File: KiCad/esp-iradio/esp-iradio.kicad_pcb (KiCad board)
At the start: 4 copper layers, 90 x 60 mm, 120 parts, among them J201 USB-C TYPE-C-31-M-12, J202 Li-Po cell (JST-PH), J3 Display HS20S010B CN1, J4 microSD push-push TF-01A, J5 Line out 3.5mm PJ-320D, J6 Speaker 4-8 Ohm, J7 Display CN2 (mechanical), Q201 MMBT3904, Q202 MMBT3904, Q203 DMG2305UX-7, SW1 EC11 with switch, SW201 RESET, SW202 BOOT, SW203 ON/OFF MSK12C02, U1 PCM5102APWR, U2 MAX98357AETE+T, U201 BQ24074RGTR, U202 USBLC6-2SC6, U203 CH340C, U204 DW01A, U205 FS8205A, U206 AP7361C-33Y5-13, U207 TPLP5907MFX-3.3, U3 ESP32-WROVER-IE-N16R8

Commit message: BQ24074RGTT (C2861252) for U201, one BOM line per LCSC part
Co-Authored-By: Claude Opus 5.5 <noreply@anthropic.com>
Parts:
- U201: value BQ24074RGTR -> BQ24074RGTT
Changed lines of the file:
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@@
 			)
 		)
-		(property "Value" "BQ24074RGTR"
+		(property "Value" "BQ24074RGTT"
 			(at 0 2.83 0)
 			(layer "F.Fab")
@@
 			)
 		)
-		(property "LCSC" "C54313"
+		(property "LCSC" "C2861252"
 			(at 0 0 0)
 			(layer "F.SilkS")

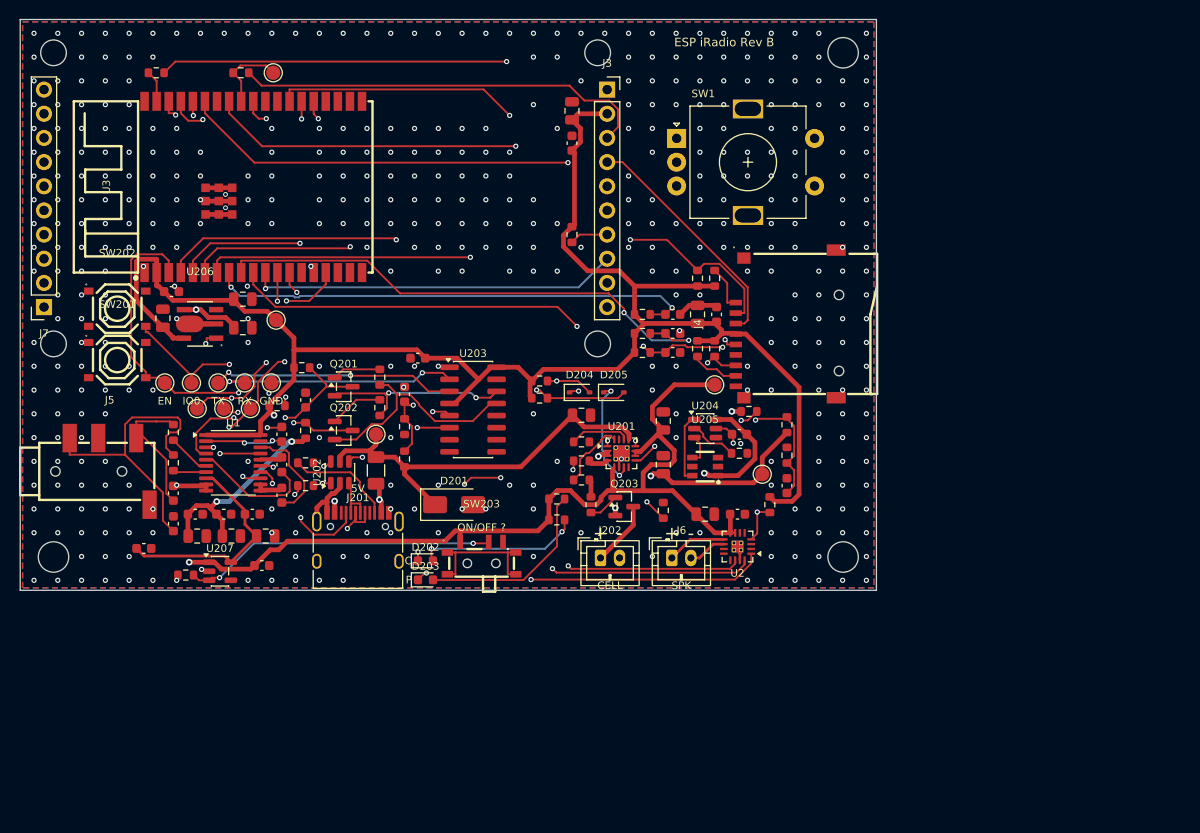
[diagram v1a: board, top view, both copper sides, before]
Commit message: KiCad Rev C: hand assembly (1206), RCA outputs, display/encoder/connectors floor plan
Co-Authored-By: Claude Opus 5.5 <noreply@anthropic.com>
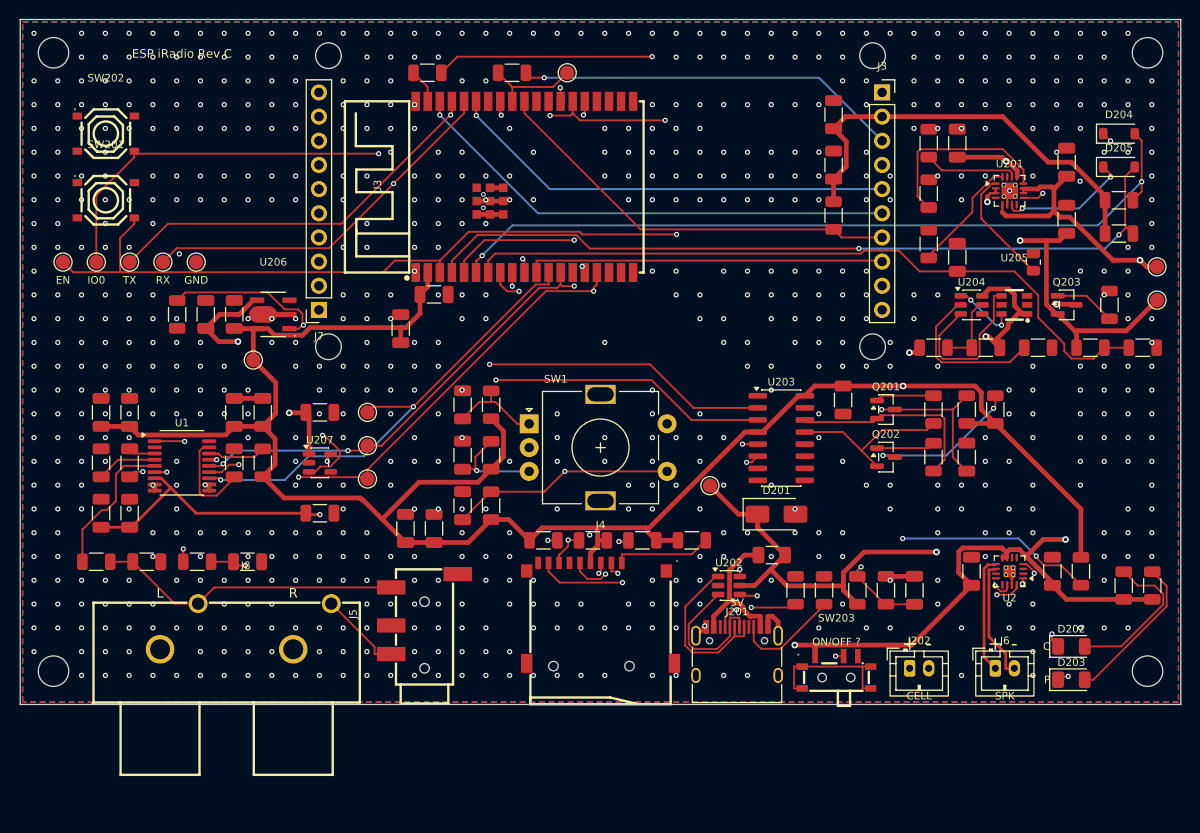
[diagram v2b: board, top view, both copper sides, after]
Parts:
- added H8: M3, MountingHole:MountingHole_3.2mm_M3, F.Cu at (103.5, 103.5)
- added J8: Line out RCA L/R AV-210-WR, lcsc:RCA-TH_AV-210-WR, F.Cu at (123.7, 163.8)
- C10, C12, C14, C201, C202, C203, C208, C209, C210, C22, C3, C5: footprint Capacitor_SMD:C_0805_2012Metric -> Capacitor_SMD:C_1206_3216Metric
- C11, C13, C15, C16, C17, C18, C19, C204, C205, C206, C207, C211, C212, C213, C214, C23, C25, C4, C6, C7, C8, C9: footprint Capacitor_SMD:C_0603_1608Metric -> Capacitor_SMD:C_1206_3216Metric
- D202, D203: footprint LED_SMD:LED_0603_1608Metric -> LED_SMD:LED_1206_3216Metric
- D204, D205: value BAT54WS -> BAT54W; footprint Diode_SMD:D_SOD-323 -> Diode_SMD:D_SOD-123
- R10, R11, R12, R15, R16, R17, R201, R202, R203, R204, R205, R206, R207, R208, R209, R21, R210, R211, R212, R213, R214, R215, R216, R217, R218, R219, R220, R221, R3, R4, R5, R6, R7, R8, R9: footprint Resistor_SMD:R_0603_1608Metric -> Resistor_SMD:R_1206_3216Metric
- RT201: footprint Resistor_SMD:R_0603_1608Metric -> Resistor_SMD:R_0805_2012Metric
- moved R208 72.5 mm to (202.5, 141.0)
- moved R207 70.0 mm to (199.5, 141.0), turned to 90 degrees
- moved C205 69.8 mm to (199.5, 146.0)
- moved D203 68.7 mm to (210.5, 169.4)
- moved D202 68.5 mm to (210.5, 165.9)
- moved R213 63.8 mm to (215.5, 119.0)
- moved R215 63.3 mm to (215.5, 122.5)
- moved R214 63.3 mm to (219.0, 159.5), turned to 90 degrees
- moved D204 62.9 mm to (215.5, 112.0)
- moved R212 60.0 mm to (216.0, 159.5), turned to 90 degrees
- moved R206 58.4 mm to (196.0, 146.0)
- moved R216 58.4 mm to (214.5, 130.0)
- moved R205 58.3 mm to (196.0, 141.0)
- moved D205 58.1 mm to (215.5, 115.5)
- moved C214 57.4 mm to (194.0, 160.0)
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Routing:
- net VSYS: track 128.2 -> 206.4 mm, vias 2 -> 5
- net +3V3: track 202.7 -> 278.2 mm, vias 3 -> 1
- net ESP_EN: track 46.3 -> 120.2 mm
- net ESP_IO0: track 60.3 -> 134.1 mm, vias 3 -> 5
- net /Power, charger and USB/VIN: track 42.9 -> 97.5 mm, vias 0 -> 2
- net Net-(U1-BCK): track 88.9 -> 133.0 mm, vias 5 -> 3
- net TXD0: track 57.3 -> 100.7 mm, vias 3 -> 2
- net Net-(C6-+): track 70.3 -> 27.7 mm, vias 2 -> 1
- net /Power, charger and USB/EN_3V3: track 59.7 -> 101.1 mm
- net Net-(U1-LRCK): track 84.8 -> 125.8 mm
- net Net-(C7-+): track 73.1 -> 32.3 mm
- net Net-(J3-Pin_4): track 76.5 -> 116.9 mm, vias 1 -> 2
- net RXD0: track 56.5 -> 92.6 mm, vias 3 -> 2
- net Net-(U1-DIN): track 91.2 -> 126.4 mm, vias 5 -> 4
- net CHG: track 50.8 -> 82.3 mm
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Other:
- board size 90 x 60 mm -> 122 x 72 mm
- board text added: "ESP iRadio Rev C"
- board text added: "L"
- board text added: "R"
- board text removed: "ESP iRadio Rev B"

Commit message: Rev C review round 7: switch off the USB-C, 1206 pitch, RCA pinout confirmed
Co-Authored-By: Claude Opus 5.5 <noreply@anthropic.com>
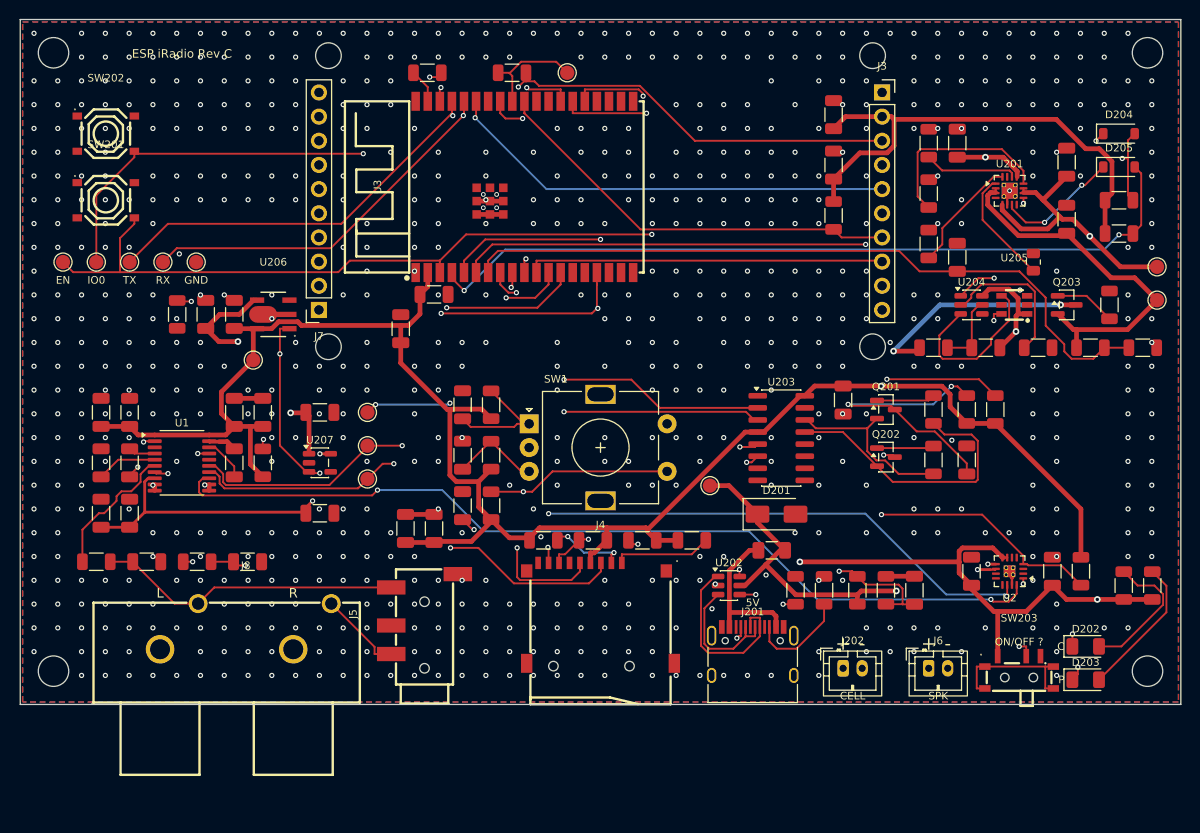
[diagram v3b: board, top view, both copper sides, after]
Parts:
- moved SW203 19.2 mm to (205.0, 168.6)
- moved J202 7.00 mm to (186.5, 168.2)
- moved J6 7.00 mm to (195.5, 168.2)
- moved J201 1.65 mm to (177.0, 167.9)
- moved D202 1.50 mm to (212.0, 165.9)
- moved D203 1.50 mm to (212.0, 169.4)
- moved F201 0.50 mm to (179.0, 155.8)
- moved C205 0.30 mm to (199.5, 146.3)
- moved R206 0.30 mm to (196.0, 146.3)
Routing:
- net /Power, charger and USB/EN_3V3: track 101.1 -> 117.8 mm, vias 3 -> 4
- net Net-(Q202-E): track 17.8 -> 30.0 mm
- net Net-(J3-Pin_4): track 116.9 -> 128.4 mm
- net ESP_IO0: track 134.1 -> 143.5 mm, vias 5 -> 4
- net Net-(U1-DIN): track 126.4 -> 135.7 mm
- net ESP_EN: track 120.2 -> 129.4 mm, vias 2 -> 3
- net Net-(C8-+): track 49.3 -> 57.8 mm, vias 2 -> 3
- net /Power, charger and USB/VIN: track 97.5 -> 90.6 mm
- net Net-(J6-Pin_2): track 12.7 -> 18.4 mm, vias 0 -> 1
- net Net-(C17-+): track 10.2 -> 4.56 mm
- net Net-(J202-Pin_1): track 54.1 -> 59.6 mm
- net Net-(J3-Pin_3): track 101.4 -> 106.6 mm
- net Net-(C15-+): track 10.5 -> 5.48 mm
- net VBUS_SENSE: track 68.9 -> 73.9 mm
- net VSYS: track 206.4 -> 211.1 mm
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
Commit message: Rev C: parts spread for hand soldering, board 122 x 76 mm
Co-Authored-By: Claude Opus 5.5 <noreply@anthropic.com>
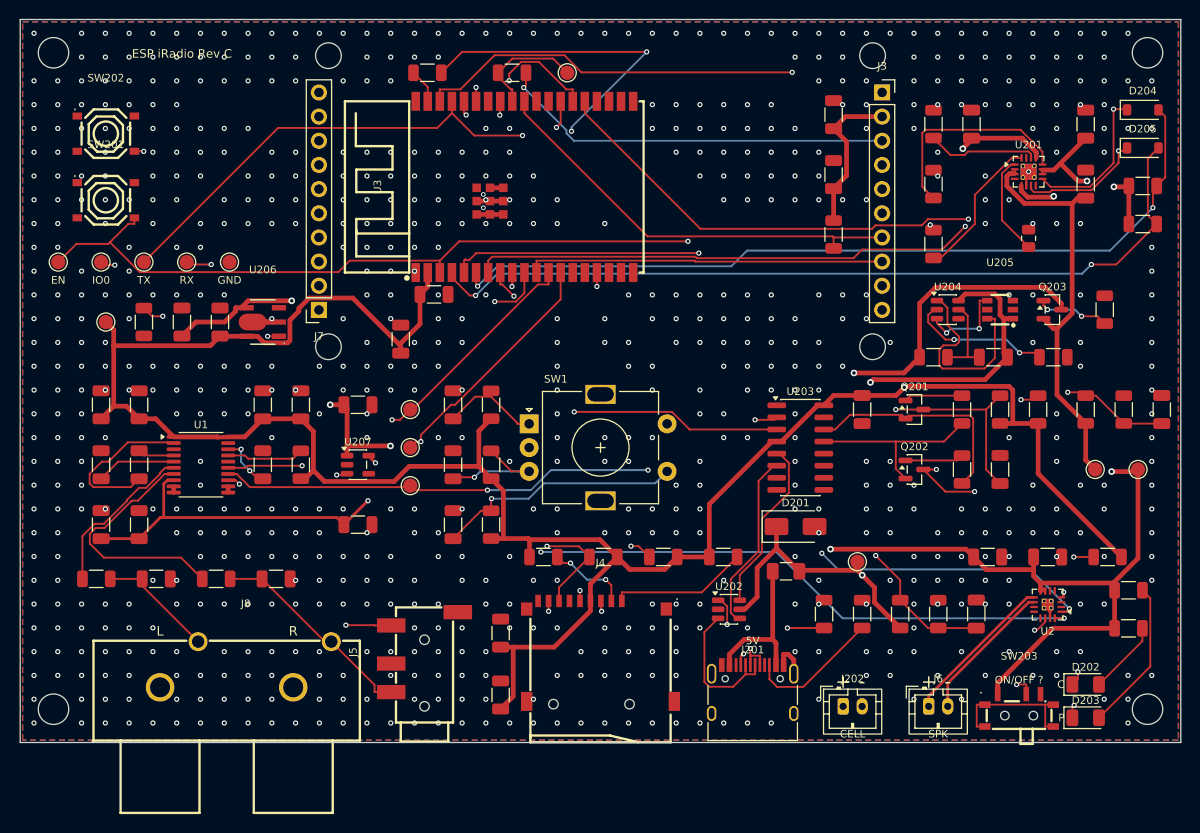
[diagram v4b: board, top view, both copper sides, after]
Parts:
- moved C207 26.8 mm to (220.0, 141.0)
- moved TP2 21.4 mm to (217.5, 147.3)
- moved TP202 18.9 mm to (213.0, 147.3)
- moved C4 18.8 mm to (150.5, 171.0)
- moved TP201 17.4 mm to (188.0, 157.0)
- moved TP4 16.0 mm to (109.0, 131.8)
- moved C3 14.9 mm to (150.5, 164.5)
- moved C214 6.96 mm to (200.5, 162.5)
- moved R218 6.80 mm to (216.0, 141.0), turned to 90 degrees
- moved R217 6.52 mm to (212.0, 141.0), turned to 90 degrees
- moved R204 6.04 mm to (196.5, 162.5)
- moved U2 5.32 mm to (208.0, 161.5)
- moved R203 5.15 mm to (192.5, 162.5)
- moved R202 4.72 mm to (188.5, 162.5)
- moved TP8 4.55 mm to (141.0, 149.0)
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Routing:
- net +3V3: track 278.2 -> 314.1 mm, vias 1 -> 2
- net /Power, charger and USB/CHG_N: track 61.0 -> 78.8 mm, vias 3 -> 2
- net Net-(U1-DIN): track 135.7 -> 121.0 mm, vias 4 -> 5
- net /Power, charger and USB/EN_3V3: track 117.8 -> 131.3 mm
- net Net-(R17-+): track 12.8 -> 25.8 mm, vias 2 -> 0
- net Net-(C15-+): track 5.48 -> 17.0 mm, vias 2 -> 0
- net Net-(U204-OD): track 10.3 -> 21.0 mm, vias 2 -> 0
- net Net-(U1-LRCK): track 123.1 -> 133.6 mm, vias 4 -> 3
- net Net-(Q202-E): track 30.0 -> 19.6 mm
- net VBUS_SENSE: track 73.9 -> 84.0 mm
- net /Power, charger and USB/PGOOD_N: track 65.4 -> 75.3 mm, vias 3 -> 2
- net ESP_IO0: track 143.5 -> 153.4 mm, vias 4 -> 6
- net VBAT_SENSE: track 76.4 -> 86.2 mm, vias 0 -> 2
- net /Power, charger and USB/USB_D+: track 19.4 -> 10.4 mm, vias 0 -> 2
- net /Power, charger and USB/BATN: track 54.1 -> 62.8 mm
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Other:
- board size 122 x 72 mm -> 122 x 76 mm

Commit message: C207 at the ADC pin (IO35), board re-routed
Co-Authored-By: Claude Opus 5.5 <noreply@anthropic.com>
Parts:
- moved C207 71.4 mm to (149.5, 129.5), turned to 0 degrees
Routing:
- net Net-(J3-Pin_4): track 119.7 -> 100.6 mm, vias 3 -> 2
- net Net-(U204-OD): track 21.0 -> 6.85 mm
- net Net-(U1-BCK): track 124.2 -> 138.3 mm
- net /Power, charger and USB/EN_3V3: track 131.3 -> 118.6 mm
- net Net-(R17-+): track 25.8 -> 13.0 mm, vias 0 -> 2
- net /Power, charger and USB/CHG_N: track 78.8 -> 66.2 mm, vias 2 -> 3
- net CHG: track 87.0 -> 97.8 mm, vias 2 -> 0
- net Net-(U1-DIN): track 121.0 -> 130.2 mm
- net Net-(J3-Pin_6): track 61.0 -> 52.1 mm
- net /Power, charger and USB/VIN: track 88.0 -> 96.8 mm, vias 2 -> 3
- net /Power, charger and USB/USB_D+: track 10.4 -> 18.9 mm, vias 2 -> 0
- net TXD0: track 101.9 -> 94.1 mm
- net /Power, charger and USB/BATN: track 62.8 -> 56.8 mm
- net Net-(Q201-E): track 24.1 -> 29.2 mm
- net VBAT_SENSE: track 86.2 -> 81.4 mm
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
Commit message: 3D models for the USB-C and the encoder (project footprints, EasyEDA models)
Co-Authored-By: Claude Opus 5.5 <noreply@anthropic.com>
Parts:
- J201: footprint Connector_USB:USB_C_Receptacle_HRO_TYPE-C-31-M-12 -> esp-iradio:USB_C_Receptacle_HRO_TYPE-C-31-M-12
- SW1: footprint Rotary_Encoder:RotaryEncoder_Alps_EC11E-Switch_Vertical_H20mm -> esp-iradio:RotaryEncoder_Alps_EC11E-Switch_Vertical_H20mm
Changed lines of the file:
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@@
 		)
 	)
-	(footprint "Connector_USB:USB_C_Receptacle_HRO_TYPE-C-31-M-12"
+	(footprint "esp-iradio:USB_C_Receptacle_HRO_TYPE-C-31-M-12"
 		(layer "F.Cu")
 		(at 177 171.9)
@@
 		)
 		(embedded_fonts no)
-		(model "${KICAD9_3DMODEL_DIR}/Connector_USB.3dshapes/USB_C_Receptacle_HRO_TYPE-C-31-M-12.step"
+		(model "${KIPRJMOD}/lib/lcsc.3dshapes/USB-C_SMD-TYPE-C-31-M-12_1.wrl"
 			(offset
-				(xyz 0 0 0)
+				(xyz 0 1.4 0)
 			)
 			(scale
@@
 			)
 			(rotate
-				(xyz 0 0 0)
+				(xyz 0 0 180)
 			)
 		)
@@
 		(embedded_fonts no)
 	)
-	(footprint "Rotary_Encoder:RotaryEncoder_Alps_EC11E-Switch_Vertical_H20mm"
+	(footprint "esp-iradio:RotaryEncoder_Alps_EC11E-Switch_Vertical_H20mm"
 		(layer "F.Cu")
 		(at 153.5 142.5)
@@
 		)
 		(embedded_fonts no)
-		(model "${KICAD9_3DMODEL_DIR}/Rotary_Encoder.3dshapes/RotaryEncoder_Alps_EC11E-Switch_Vertical_H20mm.step"
+		(model "${KIPRJMOD}/lib/lcsc.3dshapes/SW-TH_EC11XXXXXXXX-L11.7-W12.0-H24.5-P2.5-LS14.5.wrl"
 			(offset
-				(xyz 0 0 0)
+				(xyz 7.5 -2.5 0)
 			)
 			(scale
@@
 			)
 			(rotate
-				(xyz 0 0 0)
+				(xyz 0 0 -90)
 			)
 		)

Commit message: 3D: display module on J3, solid PJ-320D model
Co-Authored-By: Claude Opus 5.5 <noreply@anthropic.com>
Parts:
- J3: footprint Connector_PinSocket_2.54mm:PinSocket_1x10_P2.54mm_Vertical -> esp-iradio:PinSocket_1x10_P2.54mm_Vertical_HS20S010B
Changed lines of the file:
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@@
 		)
 	)
-	(footprint "Connector_PinSocket_2.54mm:PinSocket_1x10_P2.54mm_Vertical"
+	(footprint "esp-iradio:PinSocket_1x10_P2.54mm_Vertical_HS20S010B"
 		(layer "F.Cu")
 		(at 190.6 107.67)
@@
 			(offset
 				(xyz 0 0 0)
+			)
+			(scale
+				(xyz 1 1 1)
+			)
+			(rotate
+				(xyz 0 0 0)
+			)
+		)
+		(model "${KIPRJMOD}/lib/esp-iradio.3dshapes/HS20S010B_on_sockets.wrl"
+			(offset
+				(xyz 0 0 0)

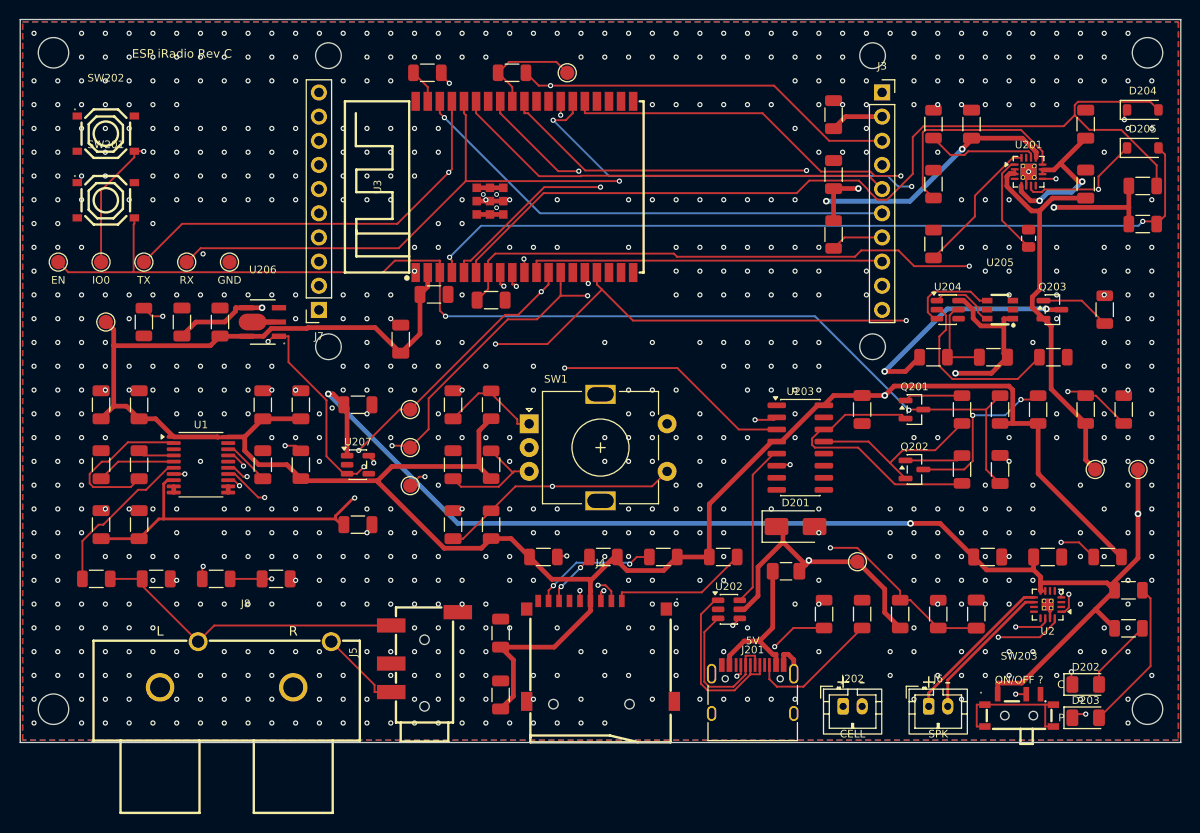
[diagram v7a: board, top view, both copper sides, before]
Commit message: Silkscreen: every reference placed next to its part; LEDs above the switch
Co-Authored-By: Claude Opus 5.5 <noreply@anthropic.com>
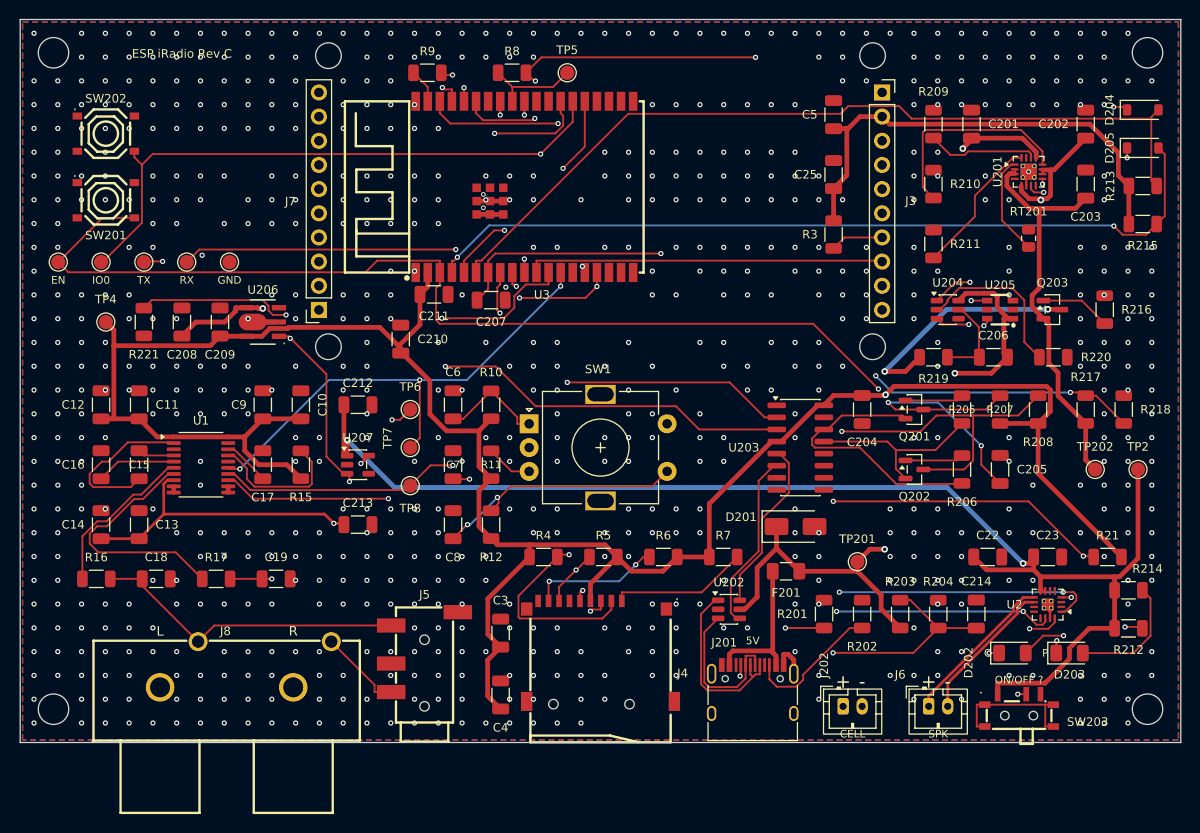
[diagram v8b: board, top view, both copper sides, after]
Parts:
- moved D202 8.38 mm to (204.3, 166.6)
- moved D203 7.01 mm to (210.3, 166.6)
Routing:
- net Net-(J4-DAT3/CD): track 59.3 -> 78.6 mm, vias 3 -> 2
- net Net-(J3-Pin_4): track 100.6 -> 115.2 mm
- net ESP_EN: track 124.3 -> 138.1 mm, vias 2 -> 3
- net /Power, charger and USB/PGOOD_N: track 74.6 -> 61.4 mm, vias 2 -> 3
- net Net-(U1-LRCK): track 134.3 -> 121.2 mm, vias 4 -> 5
- net Net-(R17-+): track 13.0 -> 25.8 mm, vias 2 -> 0
- net TXD0: track 94.1 -> 104.9 mm, vias 2 -> 3
- net CHG: track 97.8 -> 88.0 mm
- net ESP_IO0: track 149.1 -> 139.6 mm, vias 5 -> 2
- net /Power, charger and USB/VIN: track 96.8 -> 87.4 mm, vias 3 -> 2
- net Net-(J3-Pin_3): track 95.9 -> 103.1 mm, vias 2 -> 3
- net Net-(D202-A+): track 7.79 -> 13.5 mm, vias 0 -> 2
- net Net-(R15--): track 9.28 -> 14.9 mm, vias 2 -> 0
- net VSYS: track 212.6 -> 218.0 mm, vias 6 -> 4
- net Net-(C8-+): track 52.0 -> 57.1 mm, vias 2 -> 3
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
